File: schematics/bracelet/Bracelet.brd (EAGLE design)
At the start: 70 x 24 mm, 14 parts

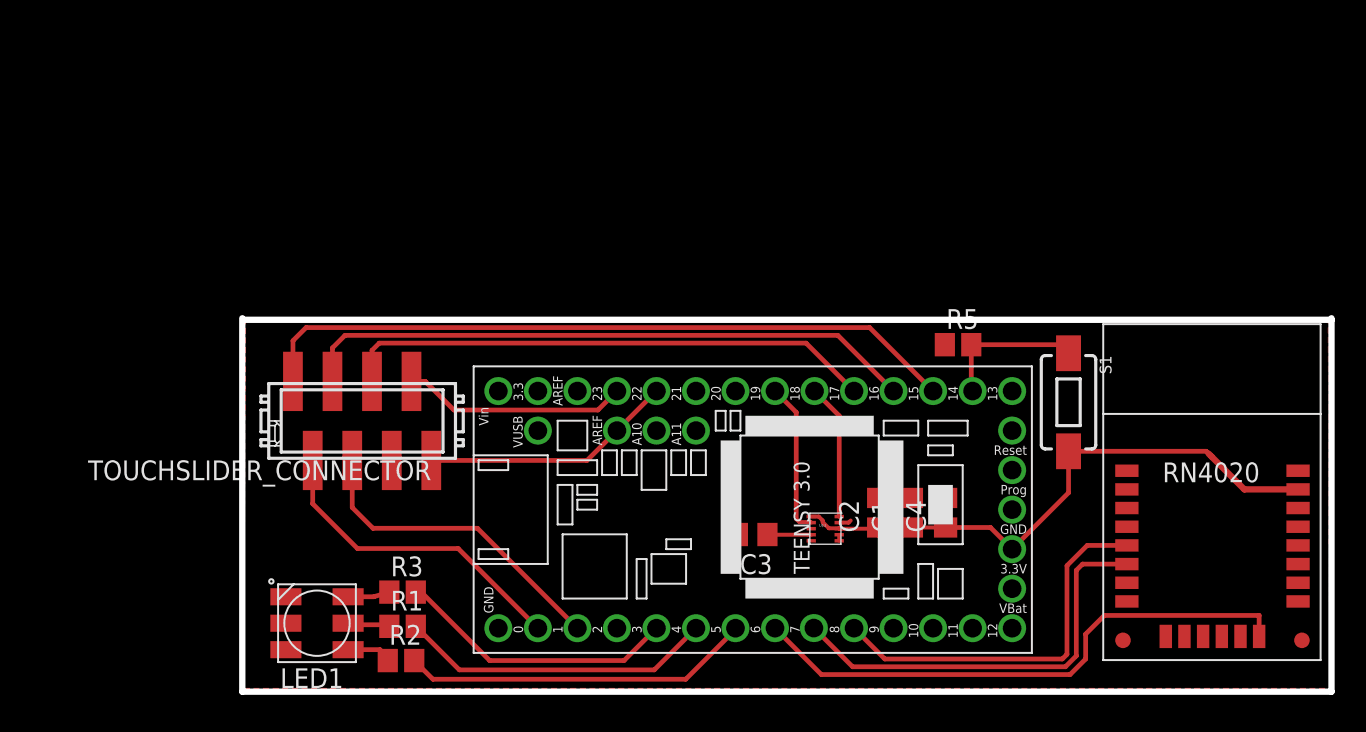
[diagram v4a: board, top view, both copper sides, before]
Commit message: new bracelet version! - new teensy only with needed pads - no button - no unnecessary multipliers at the LED - broader circuits - pcb is much smaller
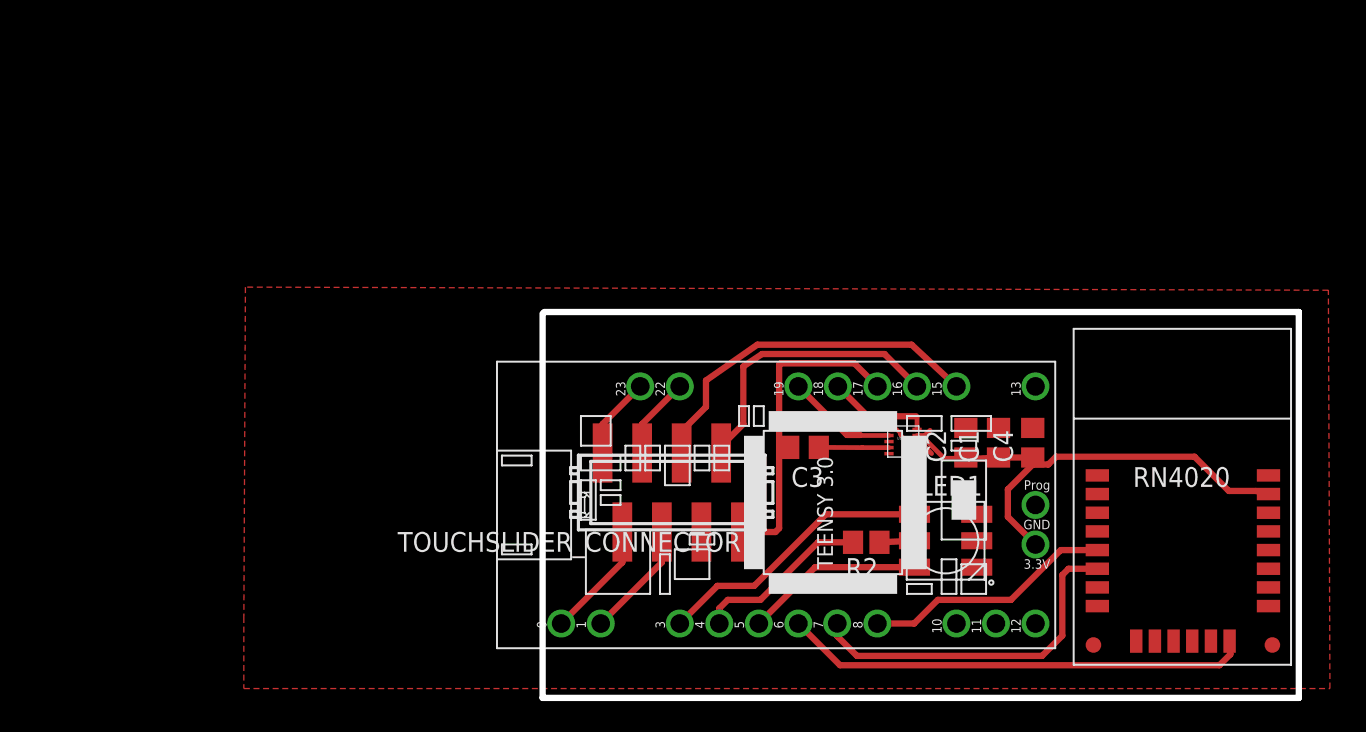
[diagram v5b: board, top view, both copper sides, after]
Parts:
- removed R1, R3, R5: (no value), resistor:R0805
- removed S1: SWITCH-MOMENTARY-2-SMD-1101NE, SparkFun-Electromechanical:TACTILE-SWITCH-1101NE
- removed U$1: TEENSY3, Teensy:TEENSY3_BRD
- added U$2: TEENSY3, teensy_minimal:TEENSY3_BRD
- moved LED1 40.7 mm to (58.2, 34.7), turned to 0 degrees
- moved R2 30.9 mm to (53.1, 34.6), turned to 180 degrees
- moved TOUCHSLIDER_CONNECTOR 20.4 mm to (40.6, 37.8)
- moved U$3 7.51 mm to (54.2, 40.1)
- moved C1 7.18 mm to (61.6, 41.0)
- moved C2 7.18 mm to (59.5, 41.0)
- moved C4 7.18 mm to (63.8, 41.0)
- moved C3 6.50 mm to (49.1, 40.7)
- moved RN4020 1.92 mm to (67.7, 28.0)
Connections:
- removed net N$5: LED1.1, R2.1
- removed net N$7: R2.2, U$1.P7
- removed net N$8: R5.2, S1.1, U$1.P16
- net +3V3: now also U$2.P30; no longer S1.2, U$1.P30
- net BLUETOOTH_TO_TEENSY: now also U$2.P10; no longer U$1.P10
- net BLUETOOTH_WAKE_HW: now also U$2.P8; no longer U$1.P8
- net CAP01: now also U$2.P25; no longer U$1.P17
- net CAP02: now also U$2.P2; no longer U$1.P2
- net CAP03: now also U$2.P24; no longer U$1.P18
- net CAP04: now also U$2.P3; no longer U$1.P3
- net CAP05: now also U$2.P17; no longer U$1.P19
- net CAP07: now also U$2.P18; no longer U$1.P25
- net CAP08: now also U$2.P19; no longer U$1.P24
- net GND: now also U$2.P32; no longer R5.1, U$1.P32
- net MISO: now also U$2.P14; no longer U$1.P14
- net MOSI: now also U$2.P13; no longer U$1.P13
- net N$2: now also LED1.2, R2.1; no longer R3.2, U$1.P5
- net N$3: now also LED1.3, U$2.P7; no longer R1.2, U$1.P6
- net N$4: now also R2.2, U$2.P6; no longer LED1.2, R1.1
- net N$6: now also LED1.1, U$2.P5; no longer LED1.3, R3.1
- net SCK: now also U$2.P15; no longer U$1.P15
- net SCL: now also U$2.P21; no longer U$1.P21
- net SDA: now also U$2.P20; no longer U$1.P20
- net SS: now also U$2.P12; no longer U$1.P12
- net TEENSY_TO_BLUETOOTH: now also U$2.P9; no longer U$1.P9
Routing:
- net CAP01: track 45.8 -> 5.28 mm
- net CAP03: track 40.0 -> 5.28 mm
- net N$7: track 22.6 -> 0.00 mm
- net N$2: track 18.1 -> 2.25 mm
- net N$6: track 2.69 -> 18.0 mm
- net CAP04: track 20.7 -> 7.51 mm
- net CAP02: track 20.6 -> 7.51 mm
- net CAP05: track 34.4 -> 23.2 mm
- net N$8: track 9.54 -> 0.00 mm
- net N$3: track 20.3 -> 11.5 mm
- net BLUETOOTH_TO_TEENSY: track 24.7 -> 16.1 mm
- net N$4: track 2.70 -> 11.3 mm
- net BLUETOOTH_WAKE_HW: track 36.2 -> 30.0 mm
- net +3V3: track 38.0 -> 33.6 mm
- net TEENSY_TO_BLUETOOTH: track 27.1 -> 22.7 mm
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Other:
- board size 70 x 24 mm -> 48.6 x 24.8 mm

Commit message: next revision for braclet board, now dual layer.
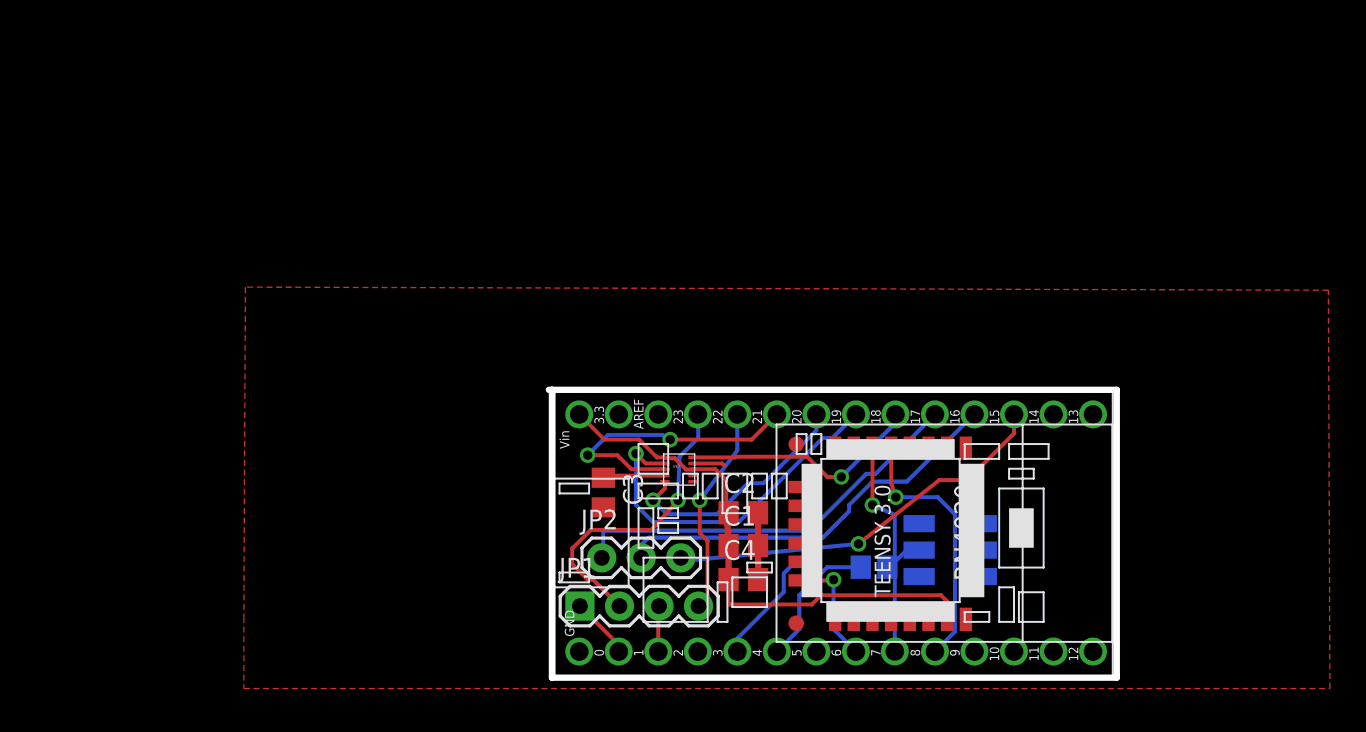
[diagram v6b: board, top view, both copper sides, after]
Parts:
- removed TOUCHSLIDER_CONNECTOR: MICROMATCH-8SMD, con-amp-micromatch-smd:MICROMATCH-8-SMD
- removed U$2: TEENSY3, teensy_minimal:TEENSY3_BRD
- added JP1: (no value), SparkFun-Connectors:1X04
- added JP2: (no value), SparkFun-Connectors:1X03
- added U$1: TEENSY3, teensy_base_compatible:TEENSY3_BRD
- moved RN4020 23.0 mm to (48.6, 40.9), turned to 270 degrees
- moved C4 20.6 mm to (45.2, 32.2), turned to 0 degrees
- moved C1 17.7 mm to (45.2, 34.4), turned to 0 degrees
- moved C2 15.0 mm to (45.2, 36.5), turned to 0 degrees
- moved U$3 14.5 mm to (39.8, 38.3)
- moved C3 13.2 mm to (36.2, 37.8), turned to 270 degrees
- moved R2 1.68 mm to (53.6, 33.0), flipped to the bottom, turned to 0 degrees
- moved LED1 0.67 mm to (58.5, 34.1), flipped to the bottom, turned to 180 degrees
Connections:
- removed net CAP08: TOUCHSLIDER_CONNECTOR.8, U$2.P19
- removed net N$3: LED1.3, U$2.P7
- new net N$5: LED1.3, U$1.P5
- net +3V3: now also U$1.P28; no longer U$2.P30
- net BLUETOOTH_TO_TEENSY: now also U$1.P10; no longer U$2.P10
- net BLUETOOTH_WAKE_HW: now also U$1.P8; no longer U$2.P8
- net CAP01: now also JP1.4, U$1.P24; no longer TOUCHSLIDER_CONNECTOR.1, U$2.P25
- net CAP02: now also JP1.3, U$1.P3; no longer TOUCHSLIDER_CONNECTOR.2, U$2.P2
- net CAP03: now also JP1.2, U$1.P25; no longer TOUCHSLIDER_CONNECTOR.3, U$2.P24
- net CAP04: now also JP1.1, U$1.P2; no longer TOUCHSLIDER_CONNECTOR.4, U$2.P3
- net CAP05: now also JP2.3, U$1.P17; no longer TOUCHSLIDER_CONNECTOR.5, U$2.P17
- net CAP06: now also JP2.2, U$1.P18; no longer TOUCHSLIDER_CONNECTOR.6
- net CAP07: now also JP2.1, U$1.P19; no longer TOUCHSLIDER_CONNECTOR.7, U$2.P18
- net GND: now also U$1.P1; no longer U$2.P32
- net INT1: now also U$1.P23
- net INT2: now also U$1.P22
- net MISO: now also U$1.P14; no longer U$2.P14
- net MOSI: now also U$1.P13; no longer U$2.P13
- net N$4: now also U$1.P6; no longer U$2.P6
- net N$6: now also U$1.P7; no longer U$2.P5
- net SCK: now also U$1.P15; no longer U$2.P15
- net SCL: now also U$1.P21; no longer U$2.P21
- net SDA: now also U$1.P20; no longer U$2.P20
- net SS: now also U$1.P12; no longer U$2.P12
- net TEENSY_TO_BLUETOOTH: now also U$1.P9; no longer U$2.P9
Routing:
- net CAP06: track 0.00 -> 26.0 mm
- net BLUETOOTH_WAKE_HW: track 30.0 -> 7.39 mm, vias 0 -> 1
- net CAP08: track 20.0 -> 0.00 mm
- net INT1: track 0.00 -> 18.8 mm, vias 0 -> 2
- net N$6: track 18.0 -> 0.00 mm
- net SCL: track 7.13 -> 22.9 mm, vias 0 -> 1
- net INT2: track 0.00 -> 15.6 mm, vias 0 -> 1
- net CAP03: track 5.28 -> 19.3 mm, vias 0 -> 1
- net N$3: track 11.5 -> 0.00 mm
- net SDA: track 6.69 -> 15.6 mm, vias 0 -> 1
- net TEENSY_TO_BLUETOOTH: track 22.7 -> 14.0 mm, vias 0 -> 1
- net CAP01: track 5.28 -> 13.6 mm, vias 0 -> 1
- net CAP07: track 18.4 -> 26.2 mm
- net N$5: track 0.00 -> 7.67 mm
- net CAP02: track 7.51 -> 2.94 mm
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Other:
- board size 48.6 x 24.8 mm -> 36.5 x 18.5 mm

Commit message: finished board layout and created gerber files.
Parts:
- moved R2 0.10 mm to (53.6, 33.1)
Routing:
- net GND: track 6.41 -> 24.1 mm, vias 0 -> 1
- net N$6: track 0.00 -> 10.2 mm, vias 0 -> 1
- net N$5: track 7.67 -> 16.3 mm
- net TEENSY_TO_BLUETOOTH: track 14.0 -> 19.1 mm
- net +3V3: track 35.0 -> 36.9 mm
- net CAP07: track 26.2 -> 27.2 mm
- net CAP05: track 25.4 -> 26.2 mm
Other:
- board size 36.5 x 18.5 mm -> 37.1 x 19.6 mm
